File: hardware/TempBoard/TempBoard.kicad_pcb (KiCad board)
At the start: 2 copper layers, 25 x 25 mm, 17 parts, among them J1 Conn_01x04, J2 Conn_01x03, U1 BME280

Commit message: finished irboard, tempboard
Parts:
- removed 3.3vTP1, GND_TP1: TestPoint, TestPoint:TestPoint_Pad_1.0x1.0mm
- added 3.3v: TestPoint, TestPoint:TestPoint_Pad_1.0x1.0mm, F.Cu at (167.7, 76.3)
- added GND: TestPoint, TestPoint:TestPoint_Pad_1.0x1.0mm, F.Cu at (171.7, 76.3)
- H1, H2, H3, H4: footprint MountingHole:MountingHole_2.2mm_M2 -> MountingHole:MountingHole_3.2mm_M3
- moved H2 126.6 mm to (179.2, 57.1)
- moved C3 114.1 mm to (170.9, 71.5), turned to 0 degrees
- moved R2 111.4 mm to (171.2, 64.3), turned to -90 degrees
- moved C1 111.3 mm to (171.7, 70.0), turned to 0 degrees
- moved C2 109.7 mm to (168.3, 70.0), turned to 180 degrees
- moved R4 108.8 mm to (173.5, 68.3), turned to 0 degrees
- moved J1 108.5 mm to (166.1, 57.4)
- moved H3 108.2 mm to (160.2, 76.1)
- moved H4 108.2 mm to (179.2, 76.1)
- moved J2 108.0 mm to (180.1, 63.9)
- moved D1 107.8 mm to (159.8, 65.5)
- moved U1 107.4 mm to (170.2, 67.7), turned to 0 degrees
- moved R3 106.8 mm to (169.7, 64.3), turned to -90 degrees
- moved R1 97.1 mm to (163.8, 65.5), turned to 180 degrees
- moved H1 90.0 mm to (160.2, 57.1)
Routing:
- net Net-(D1-A): track 23.0 -> 2.20 mm
- net GND: track 13.7 -> 6.73 mm
- net /SDA: track 30.4 -> 35.0 mm, vias 2 -> 0
- net +3.3V: track 12.1 -> 16.6 mm, vias 2 -> 6
- net /SCL: track 26.0 -> 26.4 mm, vias 2 -> 0
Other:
- board size 25 x 25 mm -> 27.1 x 27.1 mm
- board text added: "Power"
- board text removed: "I2C Test"
- board text removed: "Status"

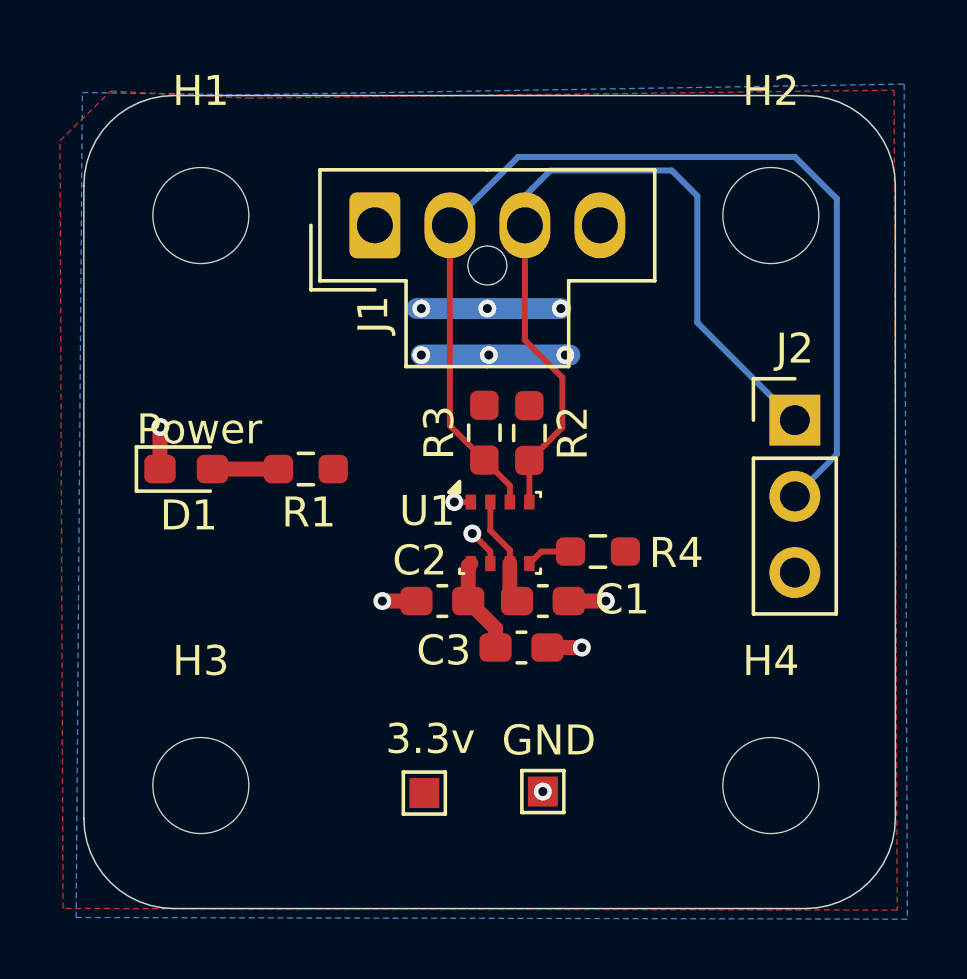
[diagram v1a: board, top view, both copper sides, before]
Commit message: finished ir_board, temp_board with horizontal connectors
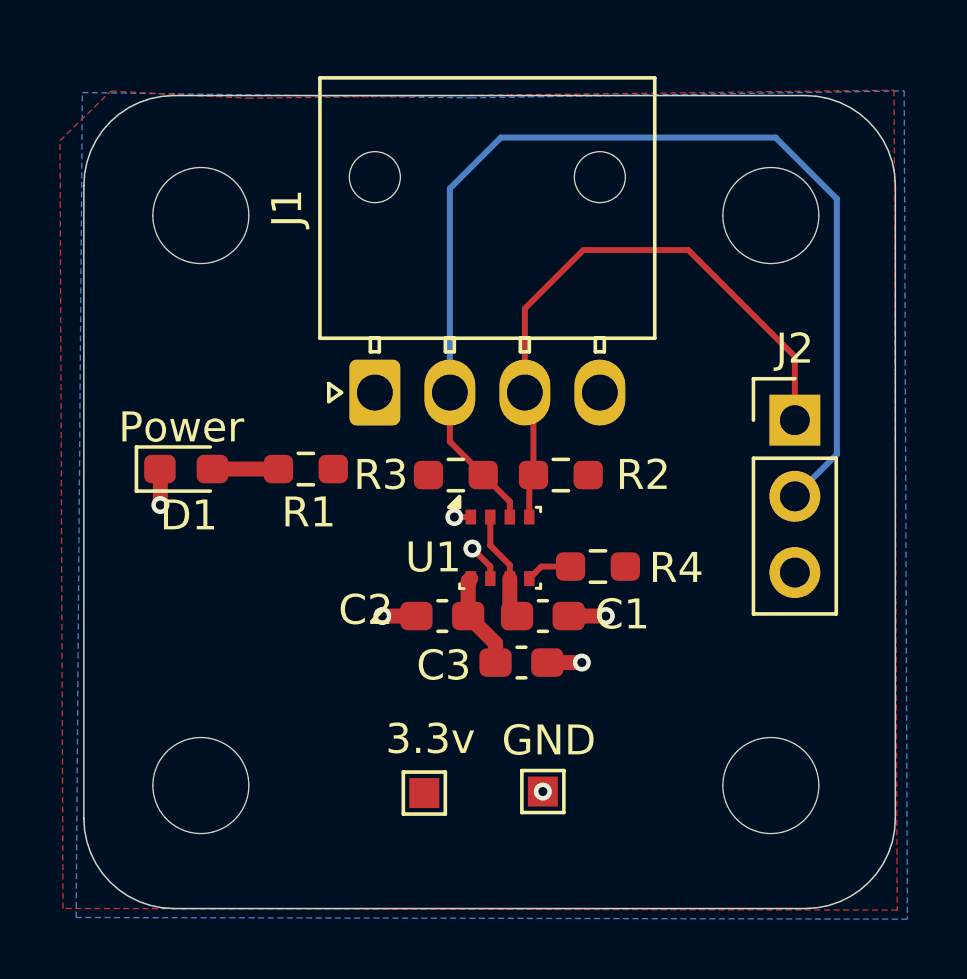
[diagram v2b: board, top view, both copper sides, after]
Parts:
- J1: footprint Connector_Molex:Molex_Nano-Fit_105309-xx04_1x04_P2.50mm_Vertical -> Connector_Molex:Molex_Nano-Fit_105313-xx04_1x04_P2.50mm_Horizontal
- moved J1 5.58 mm to (166.1, 63.0)
- moved R2 1.75 mm to (172.2, 65.8), turned to 180 degrees
- moved R3 1.70 mm to (168.8, 65.8), turned to 0 degrees
- moved C1 0.50 mm to (171.7, 70.5)
- moved C2 0.50 mm to (168.3, 70.5)
- moved C3 0.50 mm to (170.9, 72.0)
- moved R4 0.50 mm to (173.5, 68.8)
- moved U1 0.50 mm to (170.2, 68.2)
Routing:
- net +3.3V: track 16.6 -> 6.88 mm, vias 6 -> 0
- net /SCL: track 26.4 -> 20.5 mm
- net /SDA: track 35.0 -> 36.7 mm

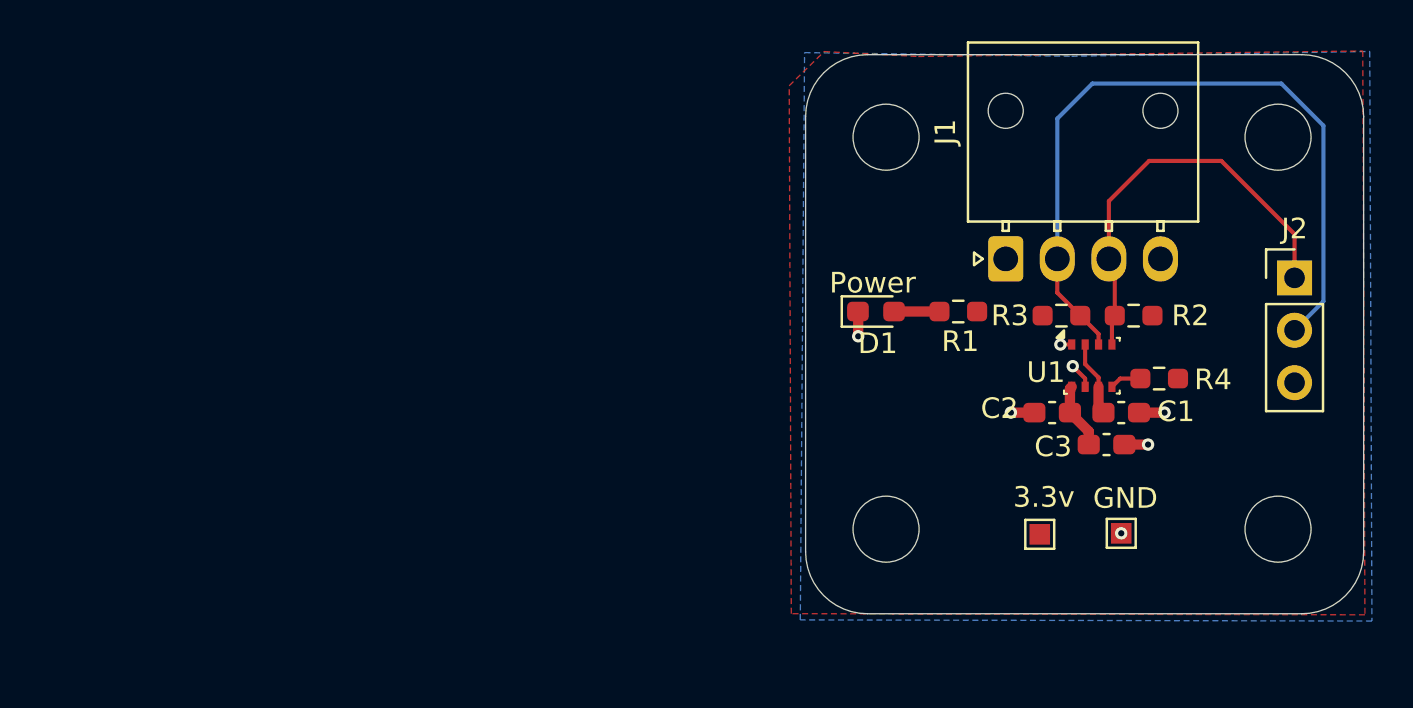
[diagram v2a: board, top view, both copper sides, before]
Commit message: Pitot Board Rev B (#3)
* init

* added layout

* ready to review

* finished pitot board

* pitot board ordered, routing+size finished for temperature board so pull??

* finished tempboard silkscreen

* resized temperature board

* poo oo ee

* ughhhhhhhhhhhhhhhhhhghghghhhhhhhhhhhhhhhhhhh

* working i2c on RH board

* cleanup?

* small

* added read me

* fixed mistake

* Fix image filename case in README.md

* Add new line for telemetry components explanation
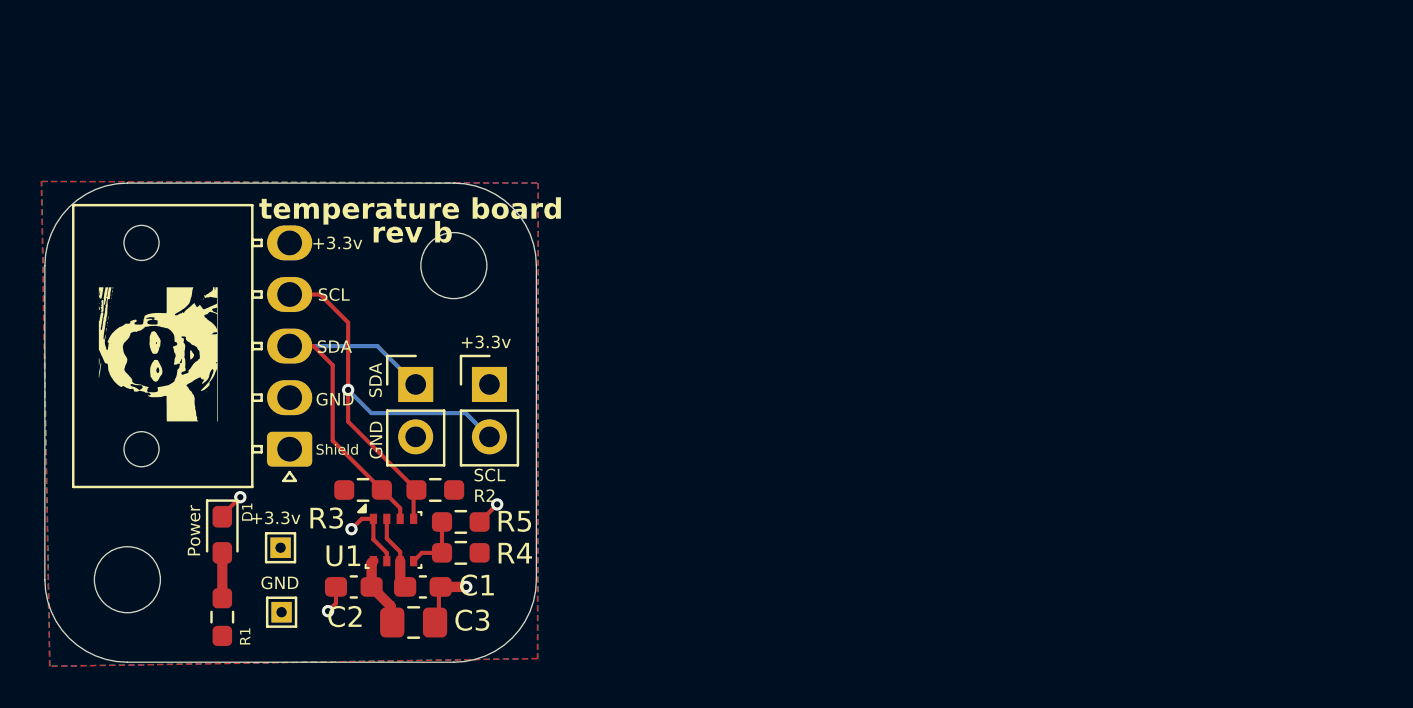
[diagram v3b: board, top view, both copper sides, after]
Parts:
- removed 3.3v, GND: TestPoint, TestPoint:TestPoint_Pad_1.0x1.0mm
- removed H3, H4: MountingHole, MountingHole:MountingHole_3.2mm_M3
- removed J2: Conn_01x03, Connector_PinHeader_2.54mm:PinHeader_1x03_P2.54mm_Vertical
- added 3.3vTP1: TestPoint, TestPoint:TestPoint_THTPad_1.0x1.0mm_Drill0.5mm, F.Cu at (130.9, 77.0)
- added G***: LOGO, custom:charlie+kirk, F.Cu at (125.0, 67.6)
- added G***: LOGO, custom:vishu, B.Cu at (127.8, 66.0)
- added G***: LOGO, custom:plane10, B.Cu at (136.1, 77.3)
- added GND_TP1: TestPoint, TestPoint:TestPoint_THTPad_1.0x1.0mm_Drill0.5mm, F.Cu at (130.9, 80.1)
- added J3: Conn_01x05, Connector_Molex:Molex_Nano-Fit_105313-xx05_1x05_P2.50mm_Horizontal, F.Cu at (131.3, 72.2)
- added J4: Conn_01x02, Connector_PinHeader_2.54mm:PinHeader_1x02_P2.54mm_Vertical, F.Cu at (137.4, 69.1)
- added R5: 0, Resistor_SMD:R_0603_1608Metric_Pad0.98x0.95mm_HandSolder, F.Cu at (139.6, 75.8)
- C3: footprint Capacitor_SMD:C_0603_1608Metric_Pad1.08x0.95mm_HandSolder -> Capacitor_SMD:C_0805_2012Metric_Pad1.18x1.45mm_HandSolder
- J1: value Conn_01x04 -> Conn_01x02; footprint Connector_Molex:Molex_Nano-Fit_105313-xx04_1x04_P2.50mm_Horizontal -> Connector_PinHeader_2.54mm:PinHeader_1x02_P2.54mm_Vertical
- R1: value 1k -> 470
- R2, R3: value 4.6k -> 10k
- moved H2 59.8 mm to (123.5, 78.5)
- moved R1 38.6 mm to (128.1, 80.4), turned to 90 degrees
- moved C2 34.9 mm to (134.4, 78.9)
- moved R4 34.9 mm to (139.6, 77.2)
- moved C1 34.9 mm to (137.8, 78.9)
- moved R2 34.9 mm to (138.4, 74.2)
- moved R3 34.9 mm to (134.9, 74.2)
- moved U1 34.9 mm to (136.4, 76.6)
- moved C3 34.7 mm to (137.3, 80.6)
- moved D1 33.5 mm to (128.1, 76.4), turned to -90 degrees
- moved J1 25.8 mm to (141.0, 69.1), turned to 0 degrees
- moved H1 21.9 mm to (139.3, 63.3)
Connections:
- J1 pad 1: GND -> +3.3V
- J1 pad 2: /SDA -> /SCL
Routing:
- net /SDA: track 36.7 -> 18.2 mm
- net GND: track 6.53 -> 10.7 mm, vias 7 -> 5
- net /SCL: track 20.5 -> 22.3 mm, vias 0 -> 1
- net Net-(U1-SDO): track 1.54 -> 3.04 mm
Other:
- board size 27.1 x 27.1 mm -> 23.8 x 23.2 mm
- board text added: "+3.3v"
- board text added: "GND"
- board text added: "SCL"
- board text added: "SDA"
- board text added: "Shield"
- board text added: "karthik kurapati febuary 2026"
- board text added: "rev b"
- board text added: "temperature board"
- board text added: "validated"
